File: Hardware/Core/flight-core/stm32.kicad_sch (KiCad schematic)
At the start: 33 parts, among them J1 Conn_01x04_Socket, J402 USB_C_Receptacle_USB2.0_16P, Q401 2N7002E, SW1 SW_SPDT, SW2 SW_MEC_5G, U1 STM32G473CCTx, U402 TCAN1042VDRQ1, U403 USBLC6-2SC6, Y1 48 MHZ

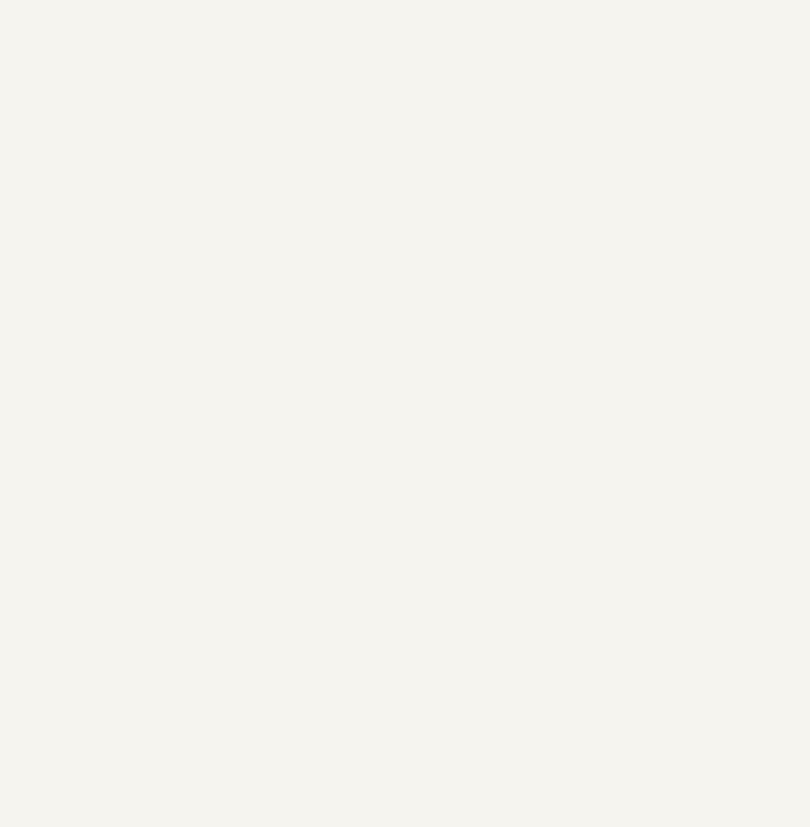
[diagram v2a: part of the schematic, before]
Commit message: adding full chain of shutdown nodes
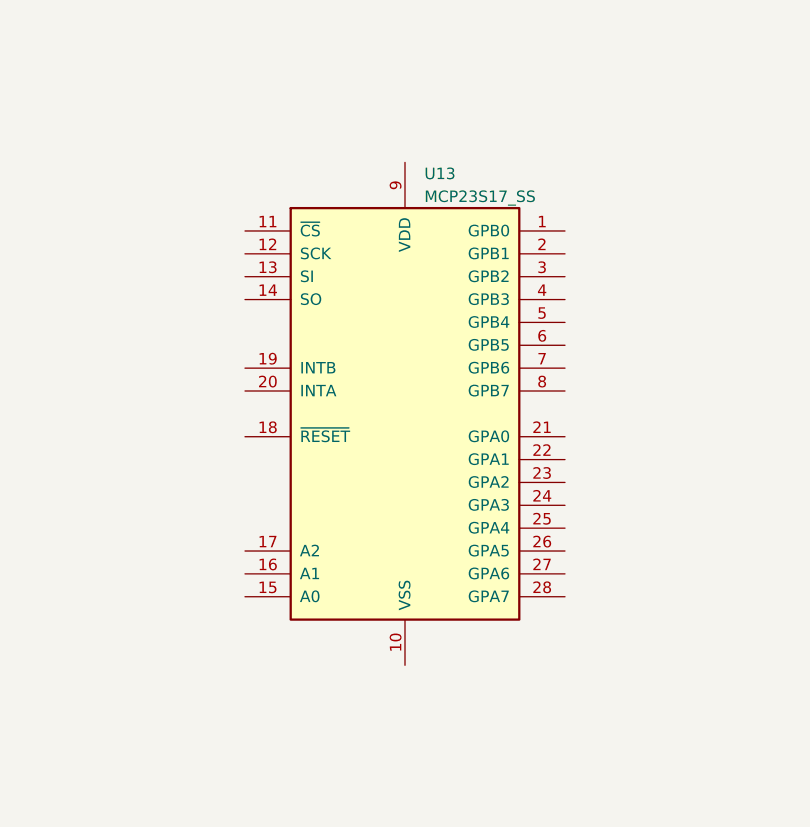
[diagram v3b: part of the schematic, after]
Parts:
- added U13: MCP23S17_SS, Package_SO:SSOP-28_5.3x10.2mm_P0.65mm, symbol Interface_Expansion:MCP23S17_SS
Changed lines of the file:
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@@
+	)
+	(symbol
+		(lib_id "Interface_Expansion:MCP23S17_SS")
+		(at 236.22 -40.64 0)
+		(unit 1)
+		(exclude_from_sim no)
+		(in_bom yes)
+		(on_board yes)
+		(dnp no)
+		(fields_autoplaced yes)
+		(property "Reference" "U13"
+			(at 238.3633 -67.31 0)
+			(effects
+				(font
+					(size 1.27 1.27)
+				)
+				(justify left)
+			)
+		)
+		(property "Value" "MCP23S17_SS"
+			(at 238.3633 -64.77 0)
+			(effects
+				(font
+					(size 1.27 1.27)
+				)
+				(justify left)
+			)
+		)
+		(property "Footprint" "Package_SO:SSOP-28_5.3x10.2mm_P0.65mm"
+			(at 241.3 -15.24 0)
+			(effects
+				(font
+					(size 1.27 1.27)
+				)
+				(justify left)
+				(hide yes)
+			)
+		)
+		(property "Datasheet" "http://ww1.microchip.com/downloads/en/DeviceDoc/20001952C.pdf"
+			(at 241.3 -12.7 0)
+			(effects
+				(font
+					(size 1.27 1.27)
+				)
+				(justify left)
+				(hide yes)
+			)
+		)
+		(property "Description" "16-bit I/O expander, SPI, interrupts, w pull-ups, SSOP-28"
+			(at 236.22 -40.64 0)
+			(effects
+				(font
+					(size 1.27 1.27)
+				)
+				(hide yes)
+			)
+		)
+		(pin "17"
+		)
+		(pin "26"
+		)
+		(pin "13"
+		)
+		(pin "14"
+		)
+		(pin "2"
+		)
+		(pin "15"
+		)
+		(pin "28"
+		)
+		(pin "16"
+		)
+		(pin "19"
+		)
+		(pin "20"
+		)
+		(pin "18"
+		)
+		(pin "11"
+		)
+		(pin "4"
+		)
+		(pin "10"
+		)
+		(pin "27"
+		)
+		(pin "22"
+		)
+		(pin "1"
+		)
+		(pin "9"
+		)
+		(pin "25"
+		)
+		(pin "5"
+		)
+		(pin "24"
+		)
+		(pin "23"
+		)
+		(pin "7"
+		)
+		(pin "6"
+		)
+		(pin "12"
+		)
+		(pin "8"
+		)
+		(pin "3"
+		)
+		(pin "21"
+		)
+		(instances
+			(project ""
+				(path "/93f46f4b-cdf5-47ec-af03-96378e73b2e1/91e18f07-bd3f-4576-bbe1-a0227cf7132e"
+					(reference "U13")
+					(unit 1)
+				)
+			)
+		)
 	)
 	(symbol

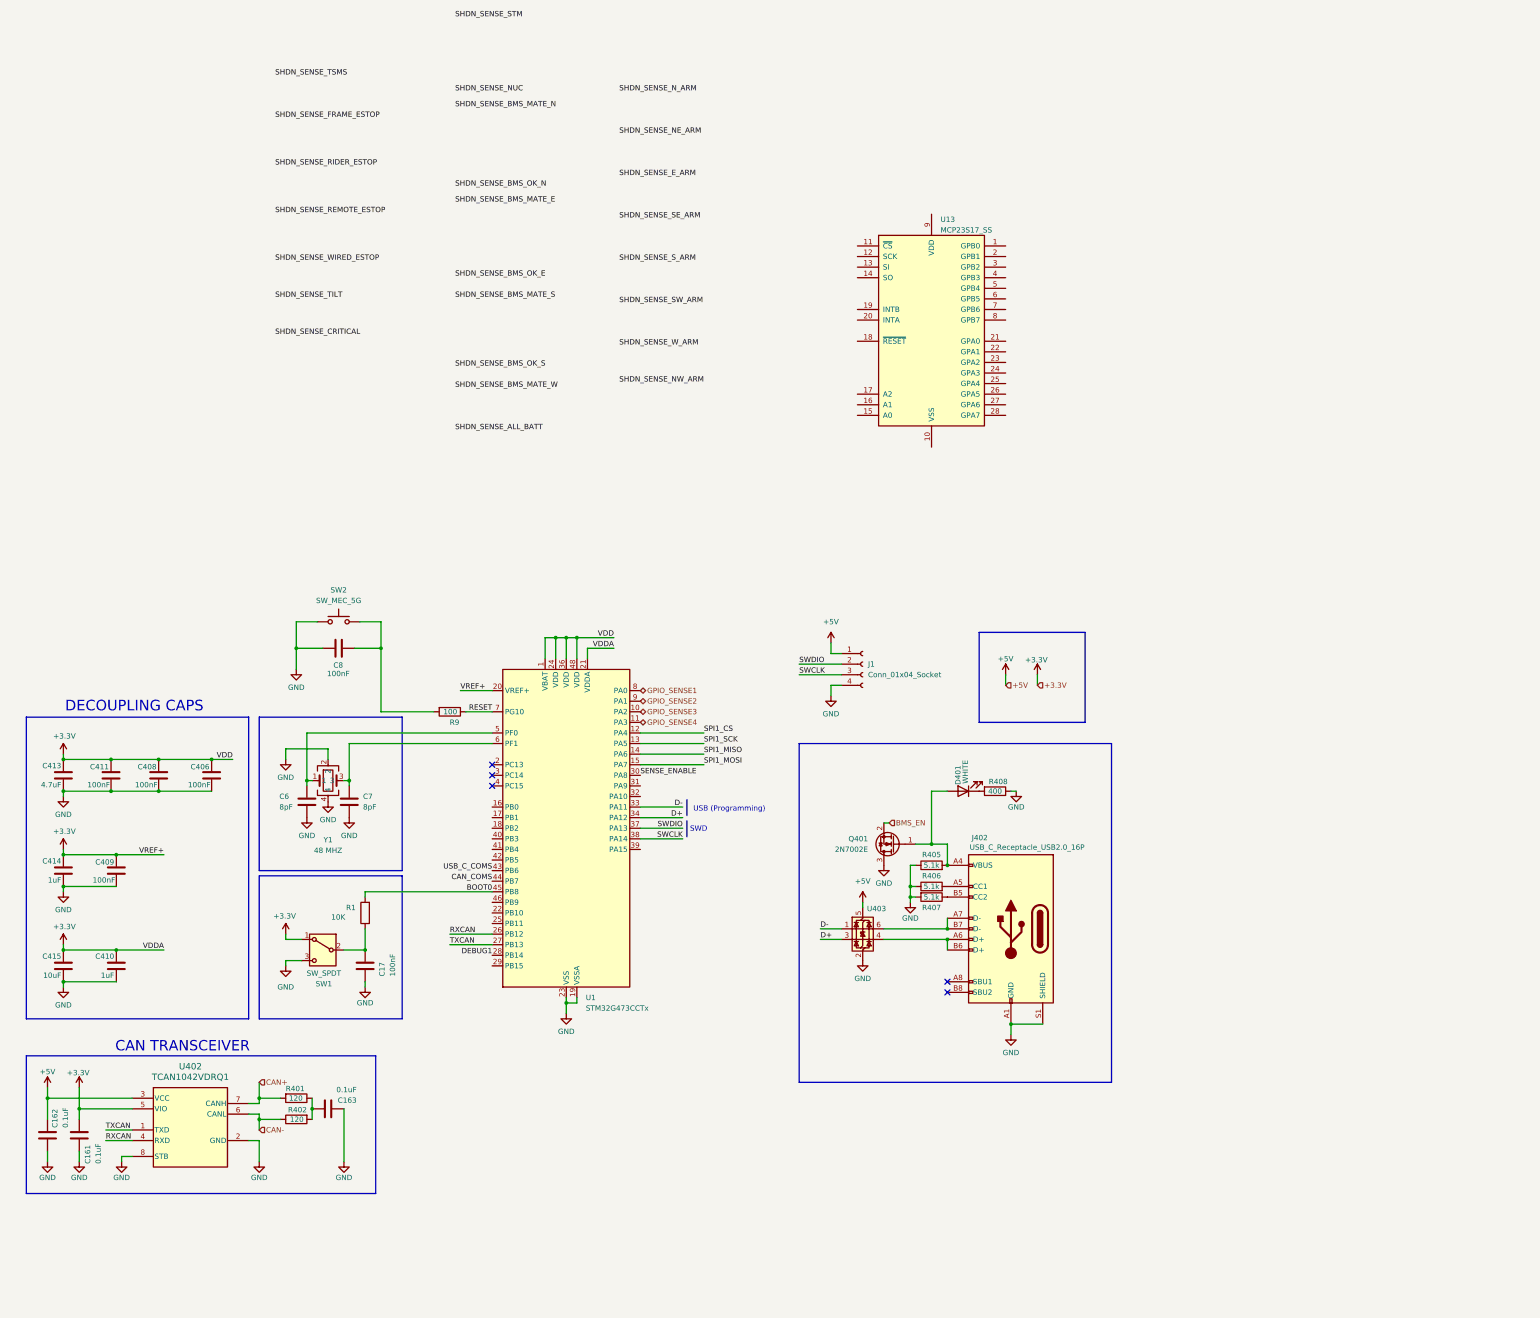
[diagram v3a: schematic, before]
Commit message: added reorganized main schematic and created draft of test_points_leds in stm32
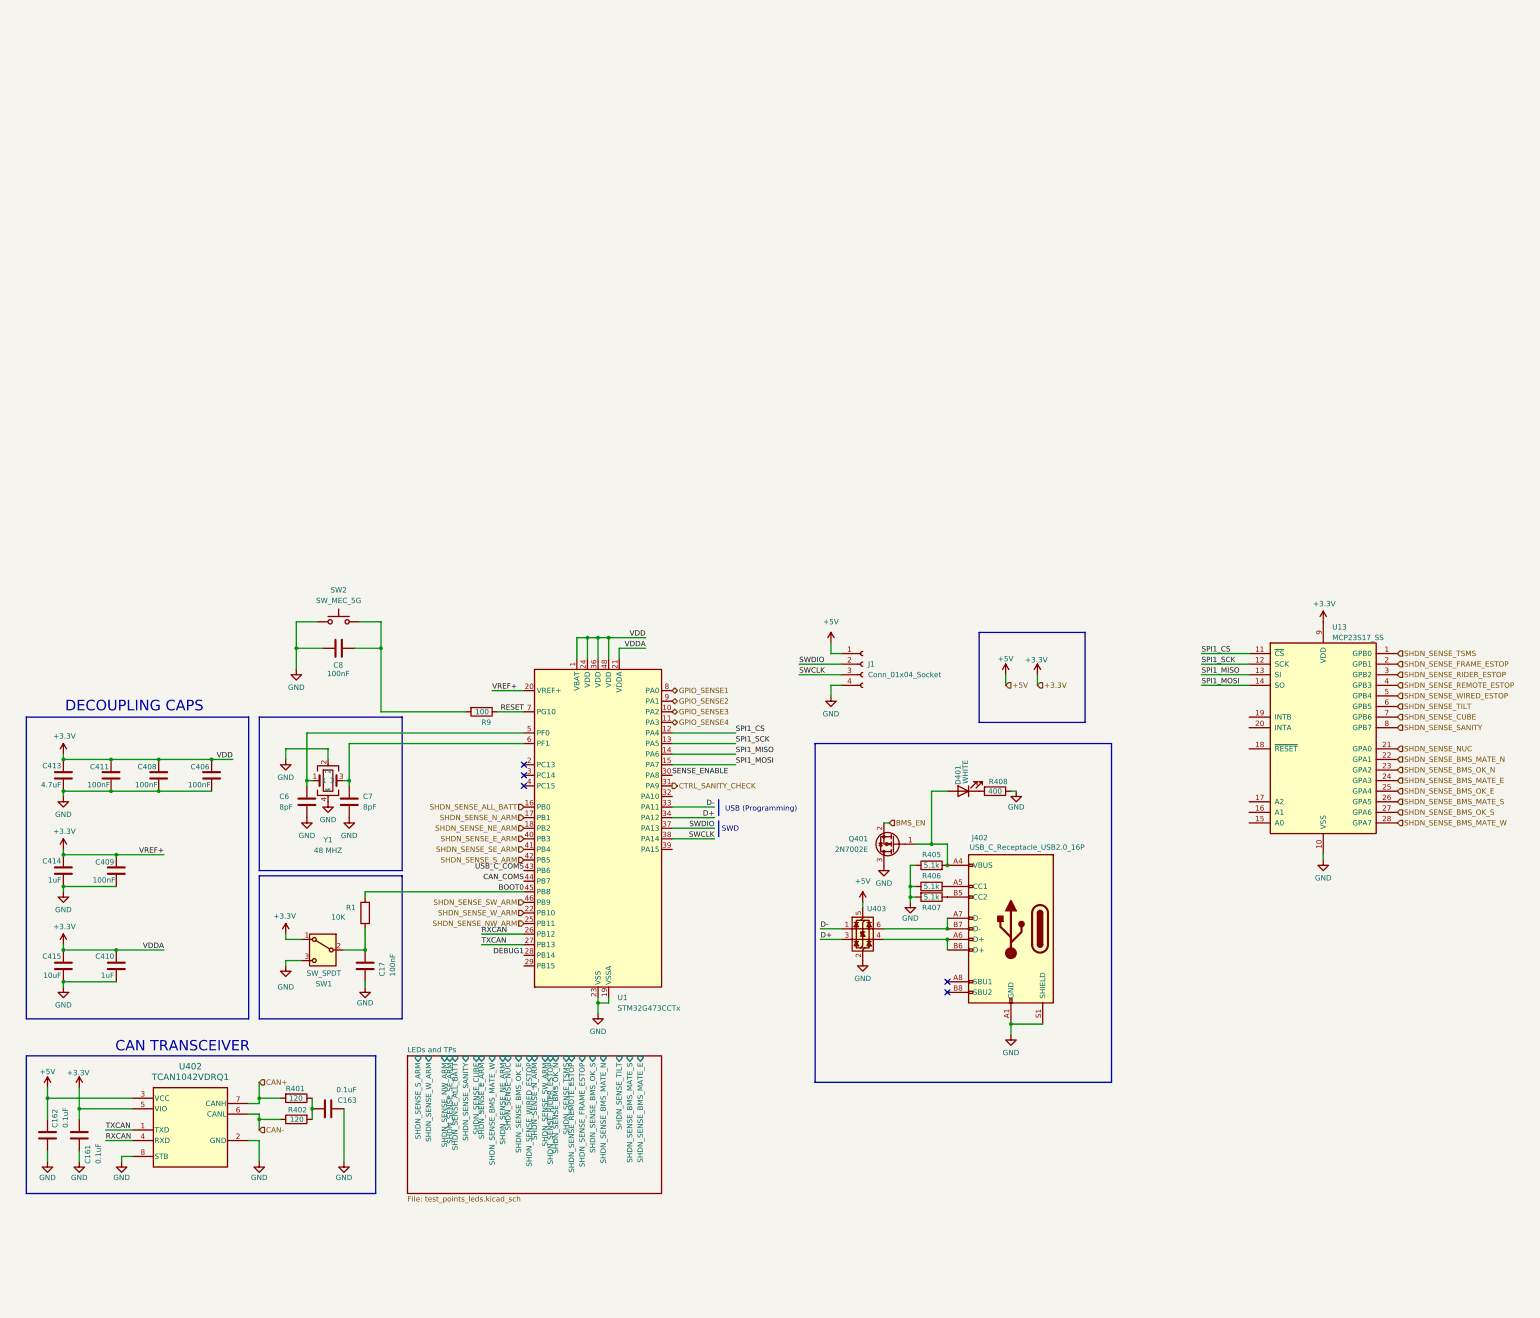
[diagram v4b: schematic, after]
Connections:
- net +3.3V: now also U13.9 (VDD)
- net GND: now also U13.10 (VSS)
- net SHDN_SENSE_ALL_BATT: now also U1.16 (PB0)
- net SHDN_SENSE_BMS_MATE_E: now also U13.24 (GPA3)
- net SHDN_SENSE_BMS_MATE_N: now also U13.22 (GPA1)
- net SHDN_SENSE_BMS_MATE_S: now also U13.26 (GPA5)
- net SHDN_SENSE_BMS_MATE_W: now also U13.28 (GPA7)
- net SHDN_SENSE_BMS_OK_E: now also U13.25 (GPA4)
- net SHDN_SENSE_BMS_OK_N: now also U13.23 (GPA2)
- net SHDN_SENSE_BMS_OK_S: now also U13.27 (GPA6)
- net SHDN_SENSE_E_ARM: now also U1.40 (PB3)
- net SHDN_SENSE_FRAME_ESTOP: now also U13.2 (GPB1)
- net SHDN_SENSE_NE_ARM: now also U1.18 (PB2)
- net SHDN_SENSE_NUC: now also U13.21 (GPA0)
- net SHDN_SENSE_NW_ARM: now also U1.25 (PB11)
- net SHDN_SENSE_N_ARM: now also U1.17 (PB1)
- net SHDN_SENSE_REMOTE_ESTOP: now also U13.4 (GPB3)
- net SHDN_SENSE_RIDER_ESTOP: now also U13.3 (GPB2)
- net SHDN_SENSE_SE_ARM: now also U1.41 (PB4)
- net SHDN_SENSE_SW_ARM: now also U1.46 (PB9)
- net SHDN_SENSE_S_ARM: now also U1.42 (PB5)
- net SHDN_SENSE_TILT: now also U13.6 (GPB5)
- net SHDN_SENSE_TSMS: now also U13.1 (GPB0)
- net SHDN_SENSE_WIRED_ESTOP: now also U13.5 (GPB4)
- net SHDN_SENSE_W_ARM: now also U1.22 (PB10)
- net SPI1_CS: now also U13.11 (~{CS})
- net SPI1_MISO: now also U13.13 (SI)
- net SPI1_MOSI: now also U13.14 (SO)
- net SPI1_SCK: now also U13.12 (SCK)
- net SHDN_SENSE_CUBE: now reaches U13.7 (GPB6)
- net SHDN_SENSE_SANITY: now reaches U13.8 (GPB7)
- net CTRL_SANITY_CHECK: now reaches U1.31 (PA9)
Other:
- added sheet LEDs and TPs (test_points_leds.kicad_sch)
- moved on the sheet: R9, U1, U13

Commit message: reorganized stm32 schematic, moved usbc to hierarchical
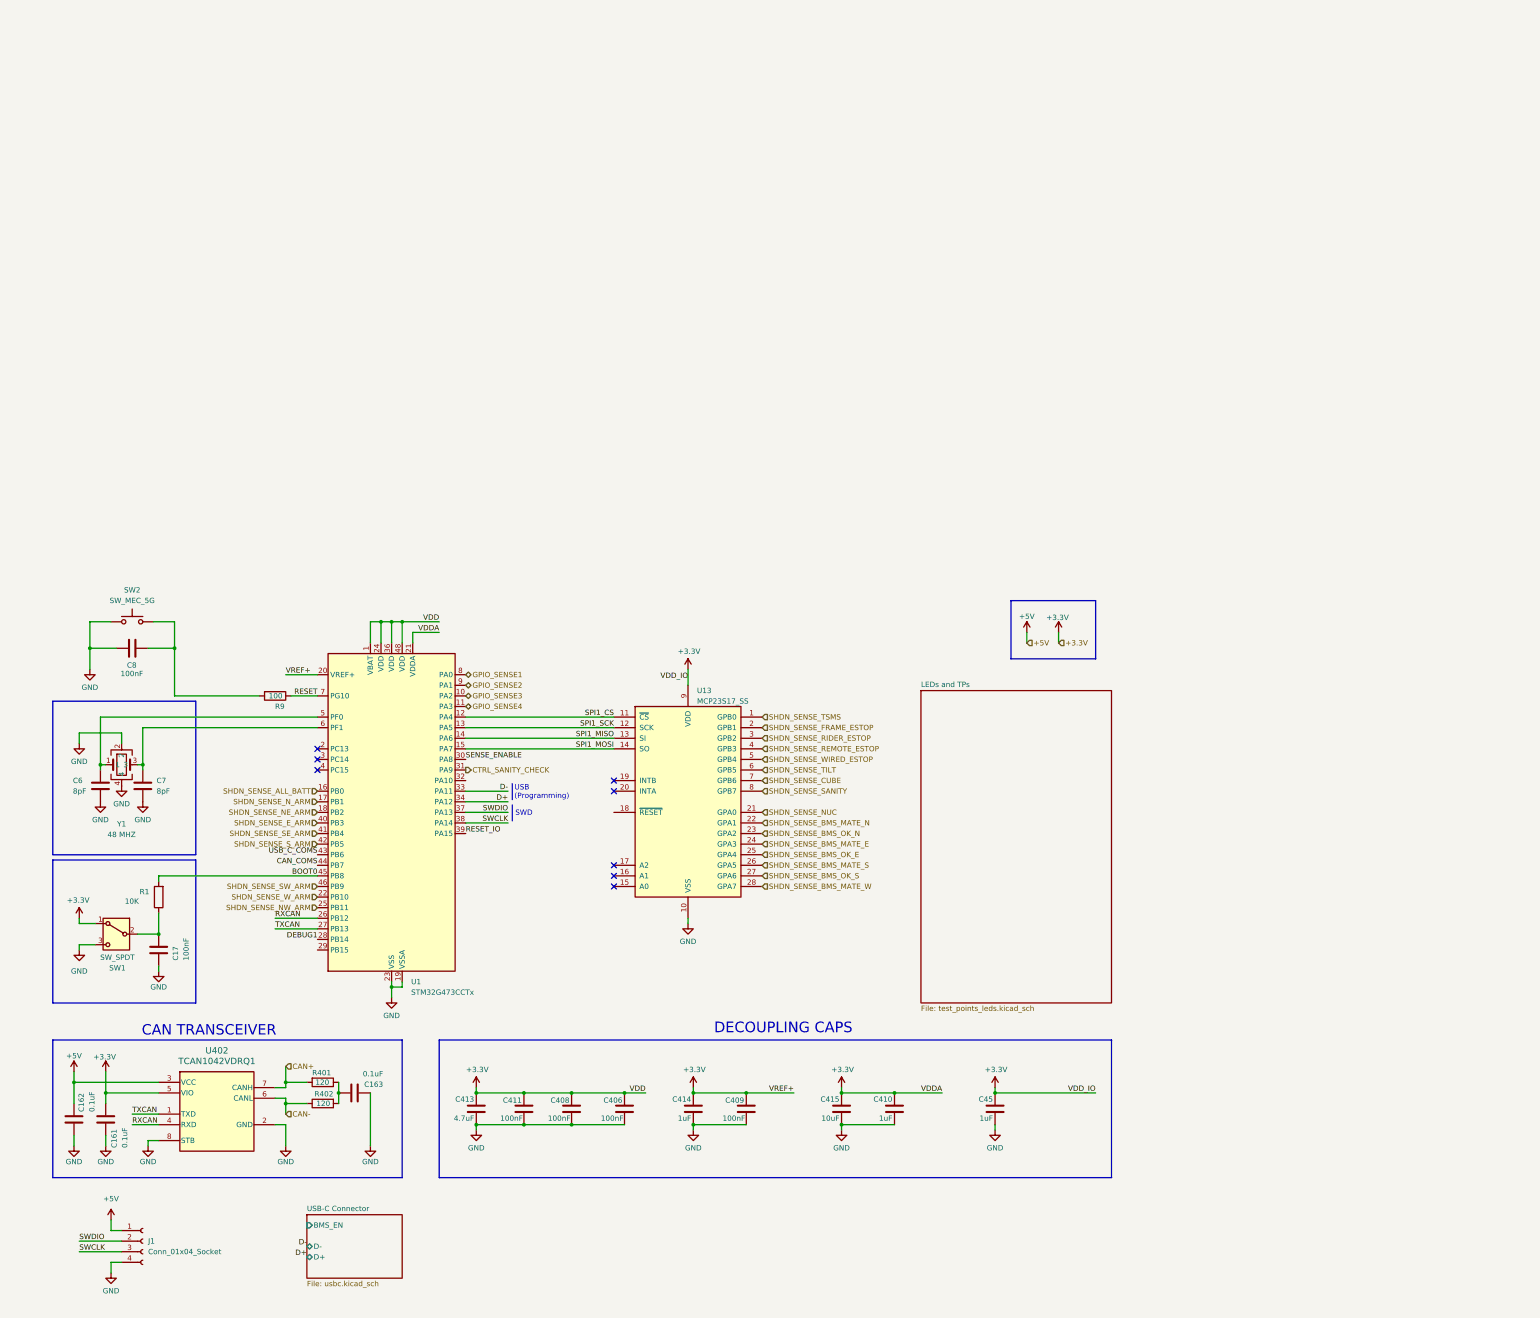
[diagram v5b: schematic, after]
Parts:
- removed D401: WHITE, LED_SMD:LED_0805_2012Metric, symbol Device:LED
- removed J402: USB_C_Receptacle_USB2.0_16P, Connector_USB:USB_C_Receptacle_G-Switch_GT-USB-7051x, symbol Connector:USB_C_Receptacle_USB2.0_16P
- removed Q401: 2N7002E, Package_TO_SOT_SMD:SOT-23, symbol Transistor_FET:2N7002E
- removed R405, R406, R407: 5.1k, OEM:R_0603_1608Metric, symbol OEM:1KR
- removed R408: 400, Resistor_SMD:R_0603_1608Metric, symbol Device:R
- removed U403: USBLC6-2SC6, Package_TO_SOT_SMD:SOT-23-6, symbol Power_Protection:USBLC6-2SC6
- added C45: 1uF, Capacitor_SMD:C_0603_1608Metric, symbol formula:C_10uF
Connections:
- net +3.3V: now also C45.1
- net GND: now also C45.2
- net RESET_IO: now reaches U1.39 (PA15)
- no-connect marks 5 -> 8
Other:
- added sheet USB-C Connector (usbc.kicad_sch)
- sheet LEDs and TPs ports: added none; removed SHDN_SENSE_ALL_BATT, SHDN_SENSE_BMS_MATE_E, SHDN_SENSE_BMS_MATE_N, SHDN_SENSE_BMS_MATE_S, SHDN_SENSE_BMS_MATE_W, SHDN_SENSE_BMS_OK_E, SHDN_SENSE_BMS_OK_N, SHDN_SENSE_BMS_OK_S, SHDN_SENSE_CUBE, SHDN_SENSE_E_ARM, SHDN_SENSE_FRAME_ESTOP, SHDN_SENSE_NE_ARM, SHDN_SENSE_NUC, SHDN_SENSE_NW_ARM, SHDN_SENSE_N_ARM, SHDN_SENSE_REMOTE_ESTOP, SHDN_SENSE_RIDER_ESTOP, SHDN_SENSE_SANITY, SHDN_SENSE_SE_ARM, SHDN_SENSE_SW_ARM, SHDN_SENSE_S_ARM, SHDN_SENSE_TILT, SHDN_SENSE_TSMS, SHDN_SENSE_WIRED_ESTOP, SHDN_SENSE_W_ARM
- moved on the sheet: C161, C162, C163, C17, C406, C408, C409, C410, C411, C413, C414, C415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
